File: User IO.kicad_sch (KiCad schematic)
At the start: 12 parts, among them SW1 SW_Push, SW2 SW_Push, SW3 SW_Push, SW4 SW_Push

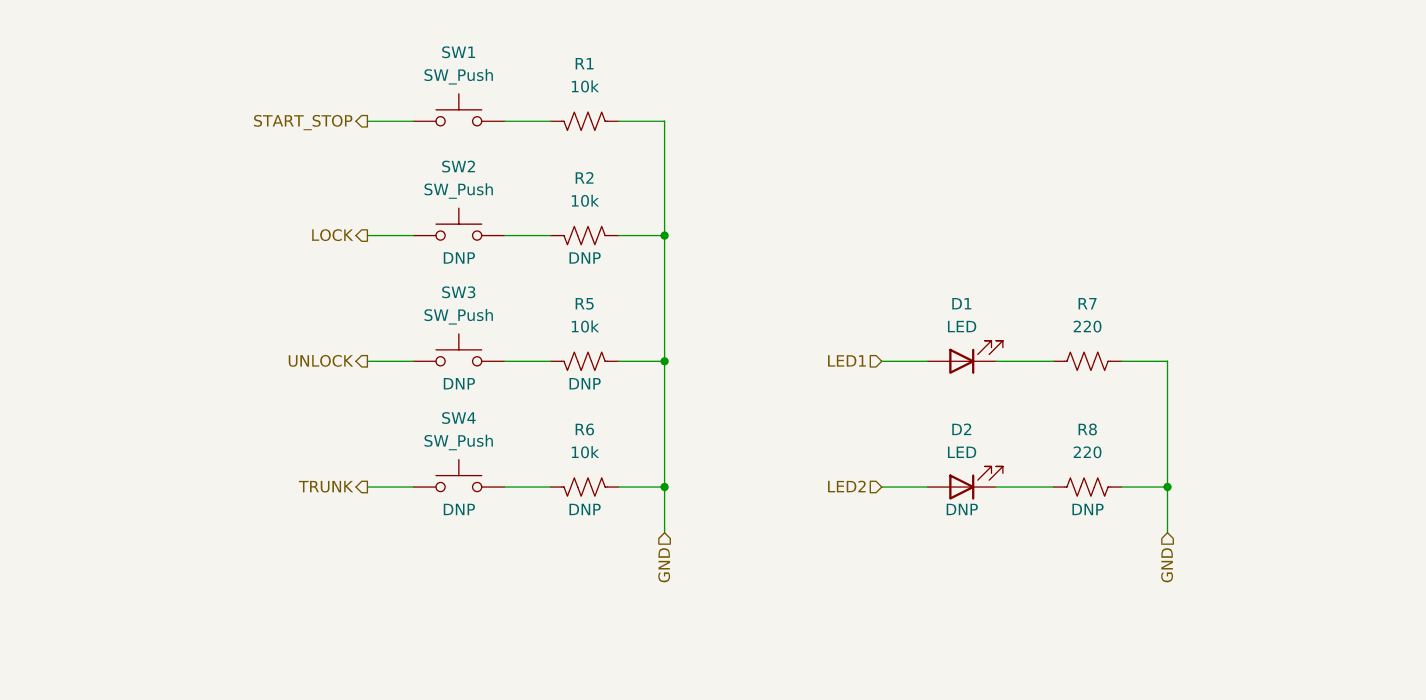
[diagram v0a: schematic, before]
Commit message: changed button to active high and added a few DNP buttons
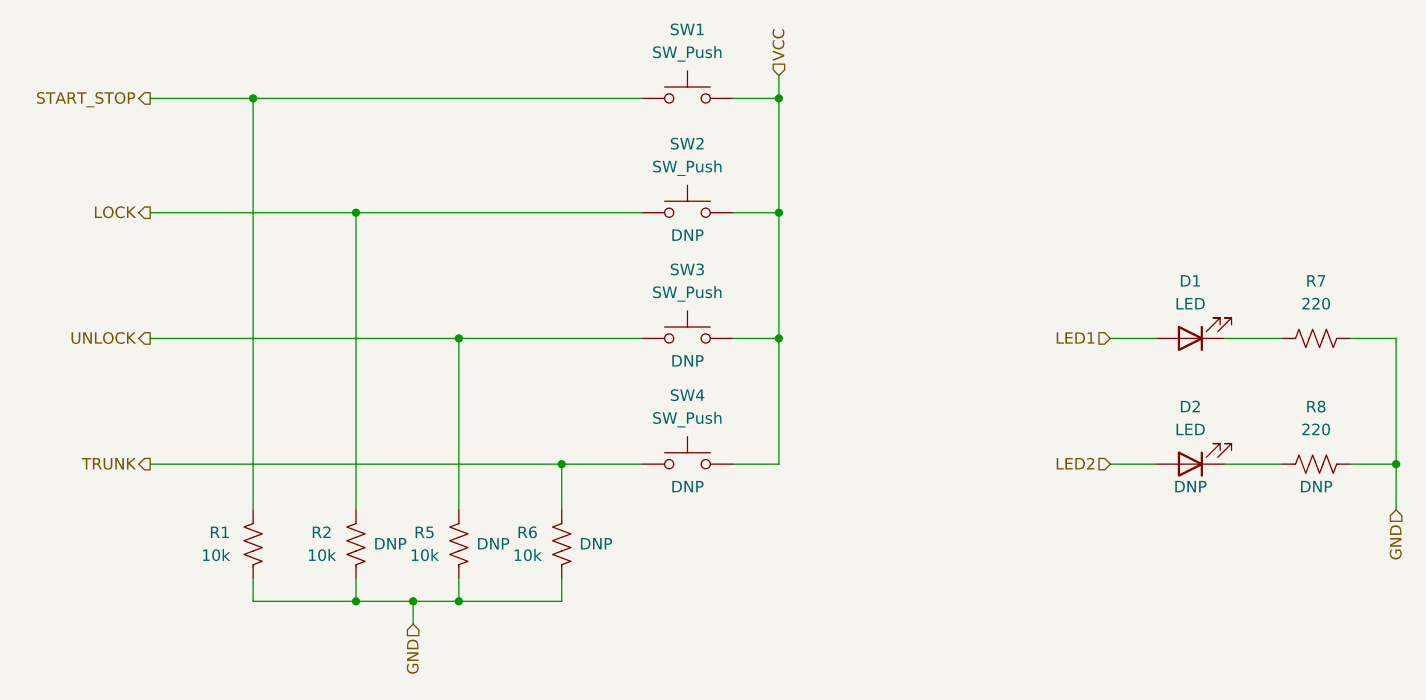
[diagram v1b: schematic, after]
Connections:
- net GND: now also R1.1, R5.1, R6.1; no longer R1.2, R5.2, R6.2
- net LOCK: now also R2.1
- net START_STOP: now also R1.2
- net TRUNK: now also R6.2
- net UNLOCK: now also R5.2
- net VCC: now reaches SW3.1
- net VCC: now also SW1.1, SW2.1, SW4.1; no longer R5.1
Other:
- moved on the sheet: D1, D2, R1, R2, R5, R6, R7, R8, SW1, SW2, SW3, SW4

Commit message: add ADC circuit, a few more DNP components, and assigned footprints
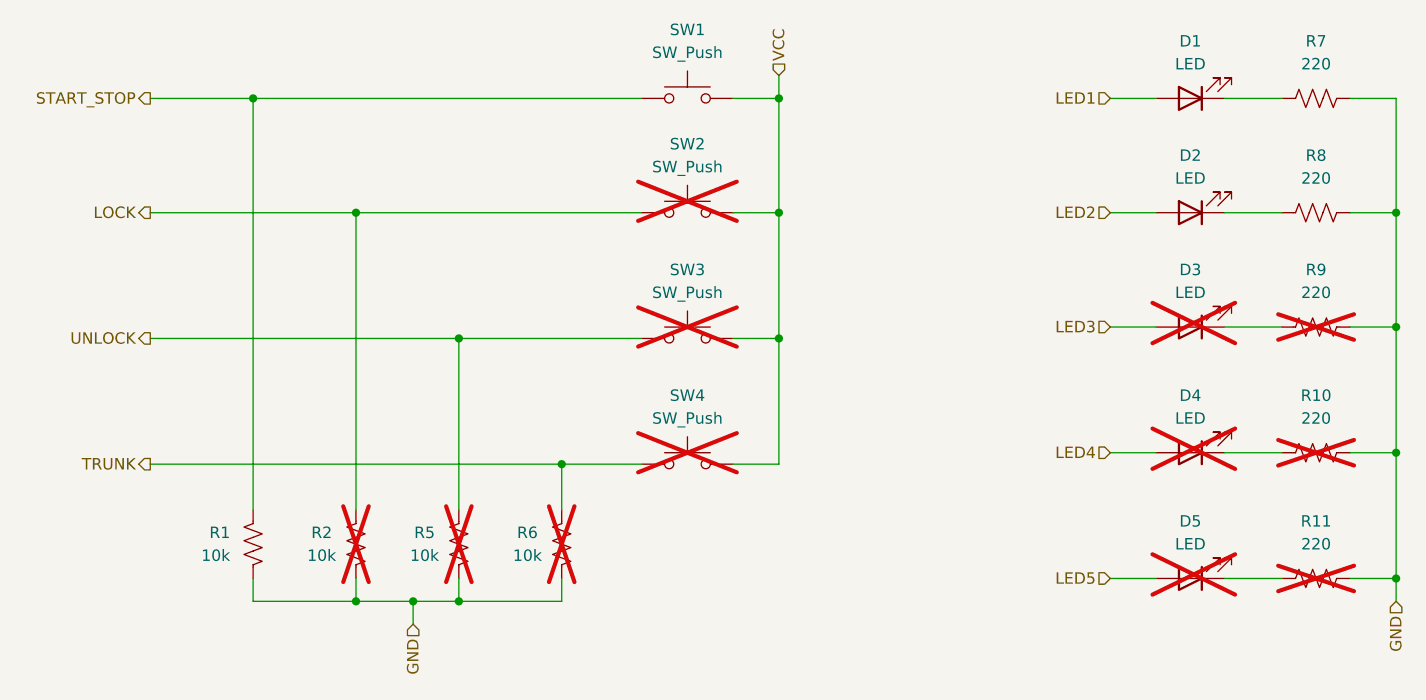
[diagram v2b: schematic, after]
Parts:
- added D3, D4, D5: LED, LED_SMD:LED_0603_1608Metric, symbol Device:LED
- added R10, R11, R9: 220, Resistor_SMD:R_0603_1608Metric, symbol Device:R_US
- D1: footprint (none) -> LED_SMD:LED_0603_1608Metric
- D2: footprint (none) -> LED_SMD:LED_0603_1608Metric; Field4 DNP -> (none)
- R1, R7: footprint (none) -> Resistor_SMD:R_0603_1608Metric
- R2, R5, R6: footprint (none) -> Resistor_SMD:R_0603_1608Metric; Field4 DNP -> (none); now not fitted
- R8: footprint (none) -> Resistor_SMD:R_0603_1608Metric; Field4 DNP -> (none)
- SW1: footprint (none) -> Button_Switch_SMD:SW_SPST_TL3305B
- SW2, SW3, SW4: footprint (none) -> Button_Switch_SMD:SW_SPST_TL3305B; Field4 DNP -> (none); now not fitted
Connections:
- net GND: now also R10.1, R11.1, R9.1
- new net: D5.1 (K), R11.2
- new net: D3.1 (K), R9.2
- new net: D4.1 (K), R10.2
- new net LED3: D3.2 (A)
- new net LED4: D4.2 (A)
- new net LED5: D5.2 (A)
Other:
- moved on the sheet: D1, D2, R7, R8

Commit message: create libraries folder for sharing external libs
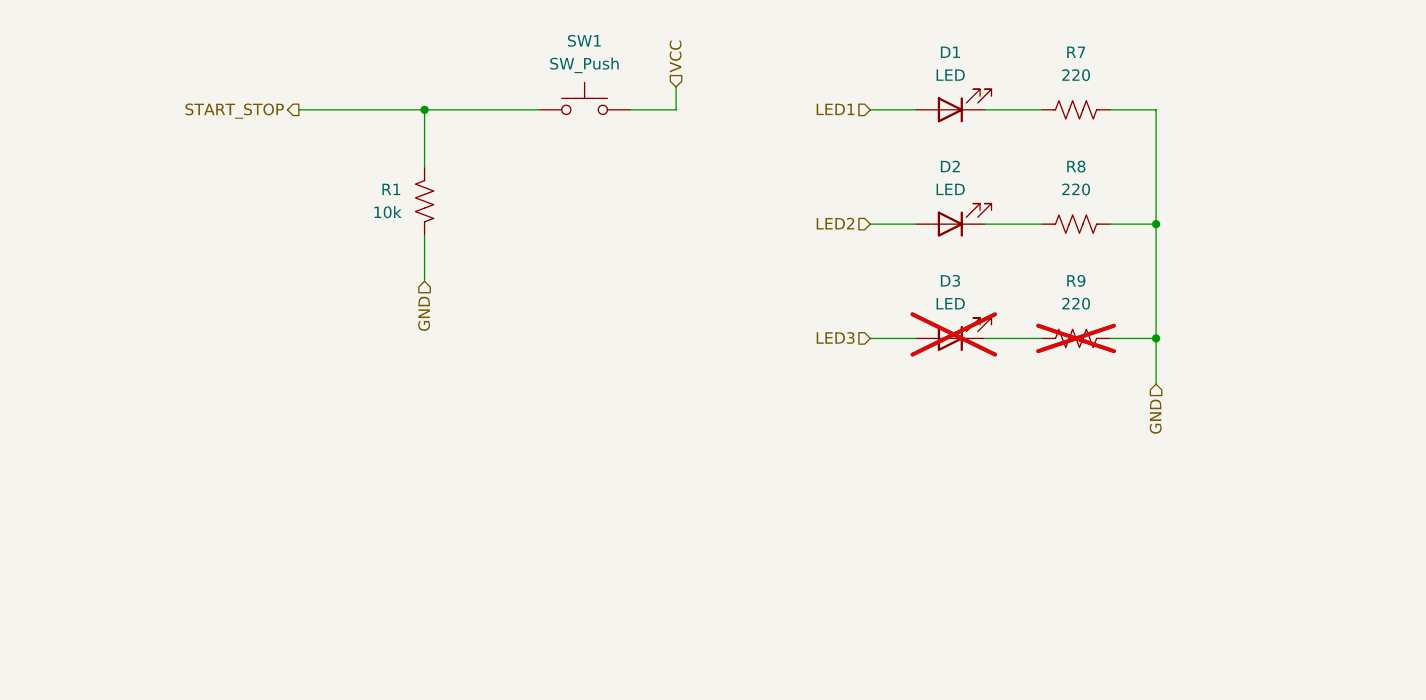
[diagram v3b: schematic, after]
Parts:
- removed D4, D5: LED, LED_SMD:LED_0603_1608Metric, symbol Device:LED
- removed R10, R11: 220, Resistor_SMD:R_0603_1608Metric, symbol Device:R_US
- removed R2, R5, R6: 10k, Resistor_SMD:R_0603_1608Metric, symbol Device:R_US
- removed SW2, SW3, SW4: SW_Push, Button_Switch_SMD:SW_SPST_TL3305B, symbol Switch:SW_Push
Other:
- moved on the sheet: D1, D2, D3, R1, R7, R8, R9, SW1

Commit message: inital layout of components complete
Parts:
- D1: value LED -> LED1
- D2: value LED -> LED2
- D3: value LED -> LED3
- SW1: value SW_Push -> START/STOP BTN
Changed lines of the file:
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@@
       (effects (font (size 1.27 1.27)))
     )
-    (property "Value" "LED" (at 173.99 68.58 0)
+    (property "Value" "LED1" (at 173.99 68.58 0)
       (effects (font (size 1.27 1.27)))
     )
@@
       (effects (font (size 1.27 1.27)))
     )
-    (property "Value" "LED" (at 173.99 93.98 0)
+    (property "Value" "LED3" (at 173.99 93.98 0)
       (effects (font (size 1.27 1.27)))
     )
@@
       (effects (font (size 1.27 1.27)))
     )
-    (property "Value" "SW_Push" (at 133.35 67.31 0)
+    (property "Value" "START/STOP BTN" (at 133.35 67.31 0)
       (effects (font (size 1.27 1.27)))
     )
@@
       (effects (font (size 1.27 1.27)))
     )
-    (property "Value" "LED" (at 173.99 81.28 0)
+    (property "Value" "LED2" (at 173.99 81.28 0)
       (effects (font (size 1.27 1.27)))
     )

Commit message: generate fab files
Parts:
- D1: MPN (none) -> C128249
- D2: MPN (none) -> C2986018
- R1: MPN (none) -> C2924175
- R7, R8: MPN (none) -> C844757
- SW1: now left out of the parts list
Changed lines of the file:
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@@
+      (effects (font (size 1.27 1.27)) hide)
+    )
+    (property "MPN" "C128249" (at 173.99 72.39 0)
       (effects (font (size 1.27 1.27)) hide)
     )
@@
       (effects (font (size 1.27 1.27)) hide)
     )
+    (property "MPN" "C844757" (at 187.96 72.39 90)
+      (effects (font (size 1.27 1.27)) hide)
+    )
     (pin "1")
     (pin "2")
@@
     )
     (property "Datasheet" "~" (at 187.96 85.09 0)
+      (effects (font (size 1.27 1.27)) hide)
+    )
+    (property "MPN" "C844757" (at 187.96 85.09 90)
       (effects (font (size 1.27 1.27)) hide)
     )
@@
       (effects (font (size 1.27 1.27)) hide)
     )
+    (property "MPN" "C2924175" (at 115.57 82.55 0)
+      (effects (font (size 1.27 1.27)) hide)
+    )
     (pin "1")
     (pin "2")
@@
   )
   (symbol (lib_id "Switch:SW_Push") (at 133.35 72.39 0) (mirror y) (unit 1)
-    (in_bom yes) (on_board yes) (dnp no) (fields_autoplaced)
+    (in_bom no) (on_board yes) (dnp no) (fields_autoplaced)
     (property "Reference" "SW1" (at 133.35 64.77 0)
       (effects (font (size 1.27 1.27)))
@@
       (effects (font (size 1.27 1.27)) hide)
     )
+    (property "MPN" "C2986018" (at 173.99 85.09 0)
+      (effects (font (size 1.27 1.27)) hide)
+    )

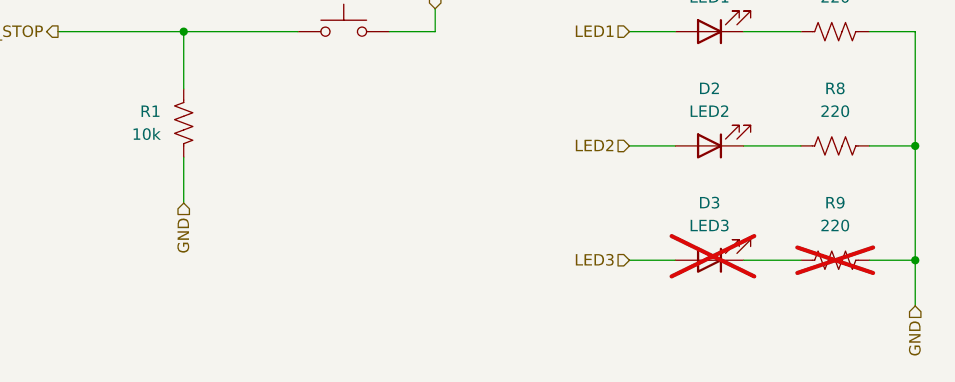
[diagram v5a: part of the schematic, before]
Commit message: replace GND heriarchical labels with GND symbols
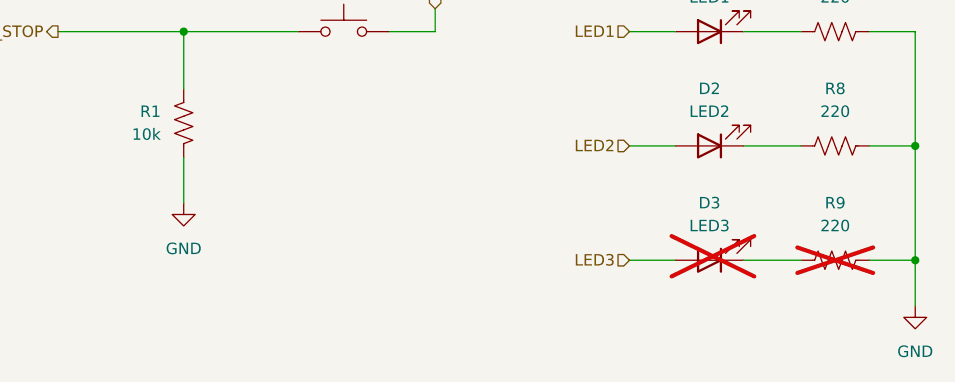
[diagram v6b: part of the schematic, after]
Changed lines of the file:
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@@
     (effects (font (size 1.27 1.27)) (justify left))
-  )
-  (hierarchical_label "GND" (shape input) (at 196.85 102.87 270) (fields_autoplaced)
-    (effects (font (size 1.27 1.27)) (justify right))
   )
   (hierarchical_label "LED1" (shape input) (at 165.1 72.39 180) (fields_autoplaced)
@@
     (effects (font (size 1.27 1.27)) (justify right))
   )
-  (hierarchical_label "GND" (shape input) (at 115.57 91.44 270) (fields_autoplaced)
-    (effects (font (size 1.27 1.27)) (justify right))
+  (symbol (lib_id "power:GND") (at 115.57 91.44 0) (unit 1)
+    (in_bom yes) (on_board yes) (dnp no) (fields_autoplaced)
+    (property "Reference" "#PWR05" (at 115.57 97.79 0)
+      (effects (font (size 1.27 1.27)) hide)
+    )
+    (property "Value" "GND" (at 115.57 96.52 0)
+      (effects (font (size 1.27 1.27)))
+    )
+    (property "Footprint" "" (at 115.57 91.44 0)
+      (effects (font (size 1.27 1.27)) hide)
+    )
+    (property "Datasheet" "" (at 115.57 91.44 0)
+      (effects (font (size 1.27 1.27)) hide)
+    )
+    (pin "1")
+    (instances
+      (project "key-fob-pcb"
+        (path "/b002c3bf-fc58-4993-80f7-7914d3aa1ac9/2e0921b6-f0d9-4f19-880e-02dc034cc8b0"
+          (reference "#PWR05") (unit 1)
+        )
+      )
+    )
+  )
+  (symbol (lib_id "power:GND") (at 196.85 102.87 0) (unit 1)
+    (in_bom yes) (on_board yes) (dnp no) (fields_autoplaced)
+    (property "Reference" "#PWR06" (at 196.85 109.22 0)
+      (effects (font (size 1.27 1.27)) hide)
+    )
+    (property "Value" "GND" (at 196.85 107.95 0)
+      (effects (font (size 1.27 1.27)))
+    )
+    (property "Footprint" "" (at 196.85 102.87 0)
+      (effects (font (size 1.27 1.27)) hide)
+    )
+    (property "Datasheet" "" (at 196.85 102.87 0)
+      (effects (font (size 1.27 1.27)) hide)
+    )
+    (pin "1")
+    (instances
+      (project "key-fob-pcb"
+        (path "/b002c3bf-fc58-4993-80f7-7914d3aa1ac9/2e0921b6-f0d9-4f19-880e-02dc034cc8b0"
+          (reference "#PWR06") (unit 1)
+        )
+      )
+    )
   )
   (symbol (lib_id "Device:LED") (at 173.99 72.39 180) (unit 1)
